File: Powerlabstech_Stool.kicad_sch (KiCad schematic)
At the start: 54 parts, among them J1 Screw_Terminal_01x02, J2 Conn_01x02_Pin, J3 Conn_01x02_Pin, J4 Conn_01x05_Socket, J5 Screw_Terminal_01x02, K1 SANYOU_SRD_Form_C, Q1 Q_NMOS_GSD, Q2 Q_NMOS_GSD, Q3 Q_NMOS_GSD, Q4 Q_NMOS_GSD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

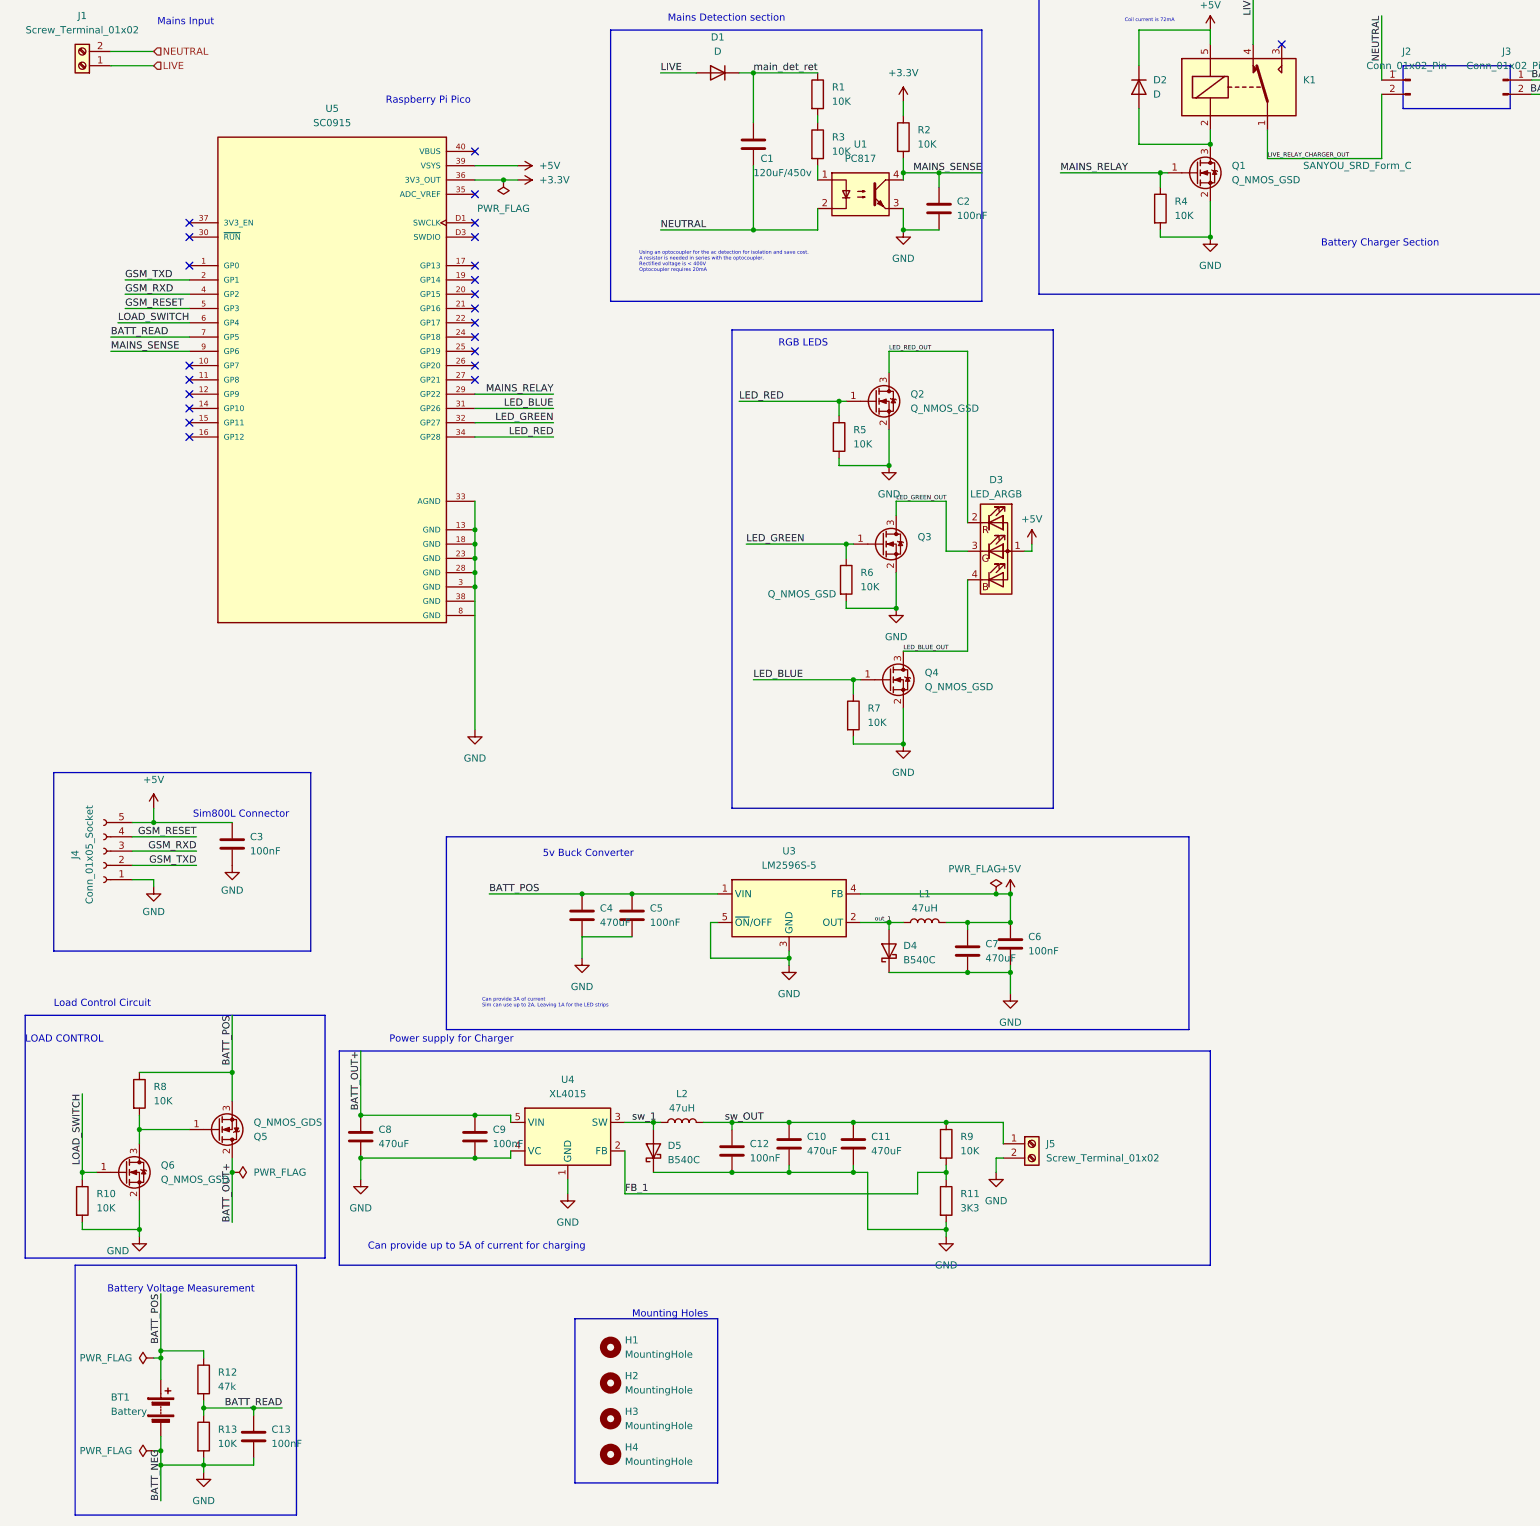
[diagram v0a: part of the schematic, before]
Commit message: Modified USB type C to supply 3A current
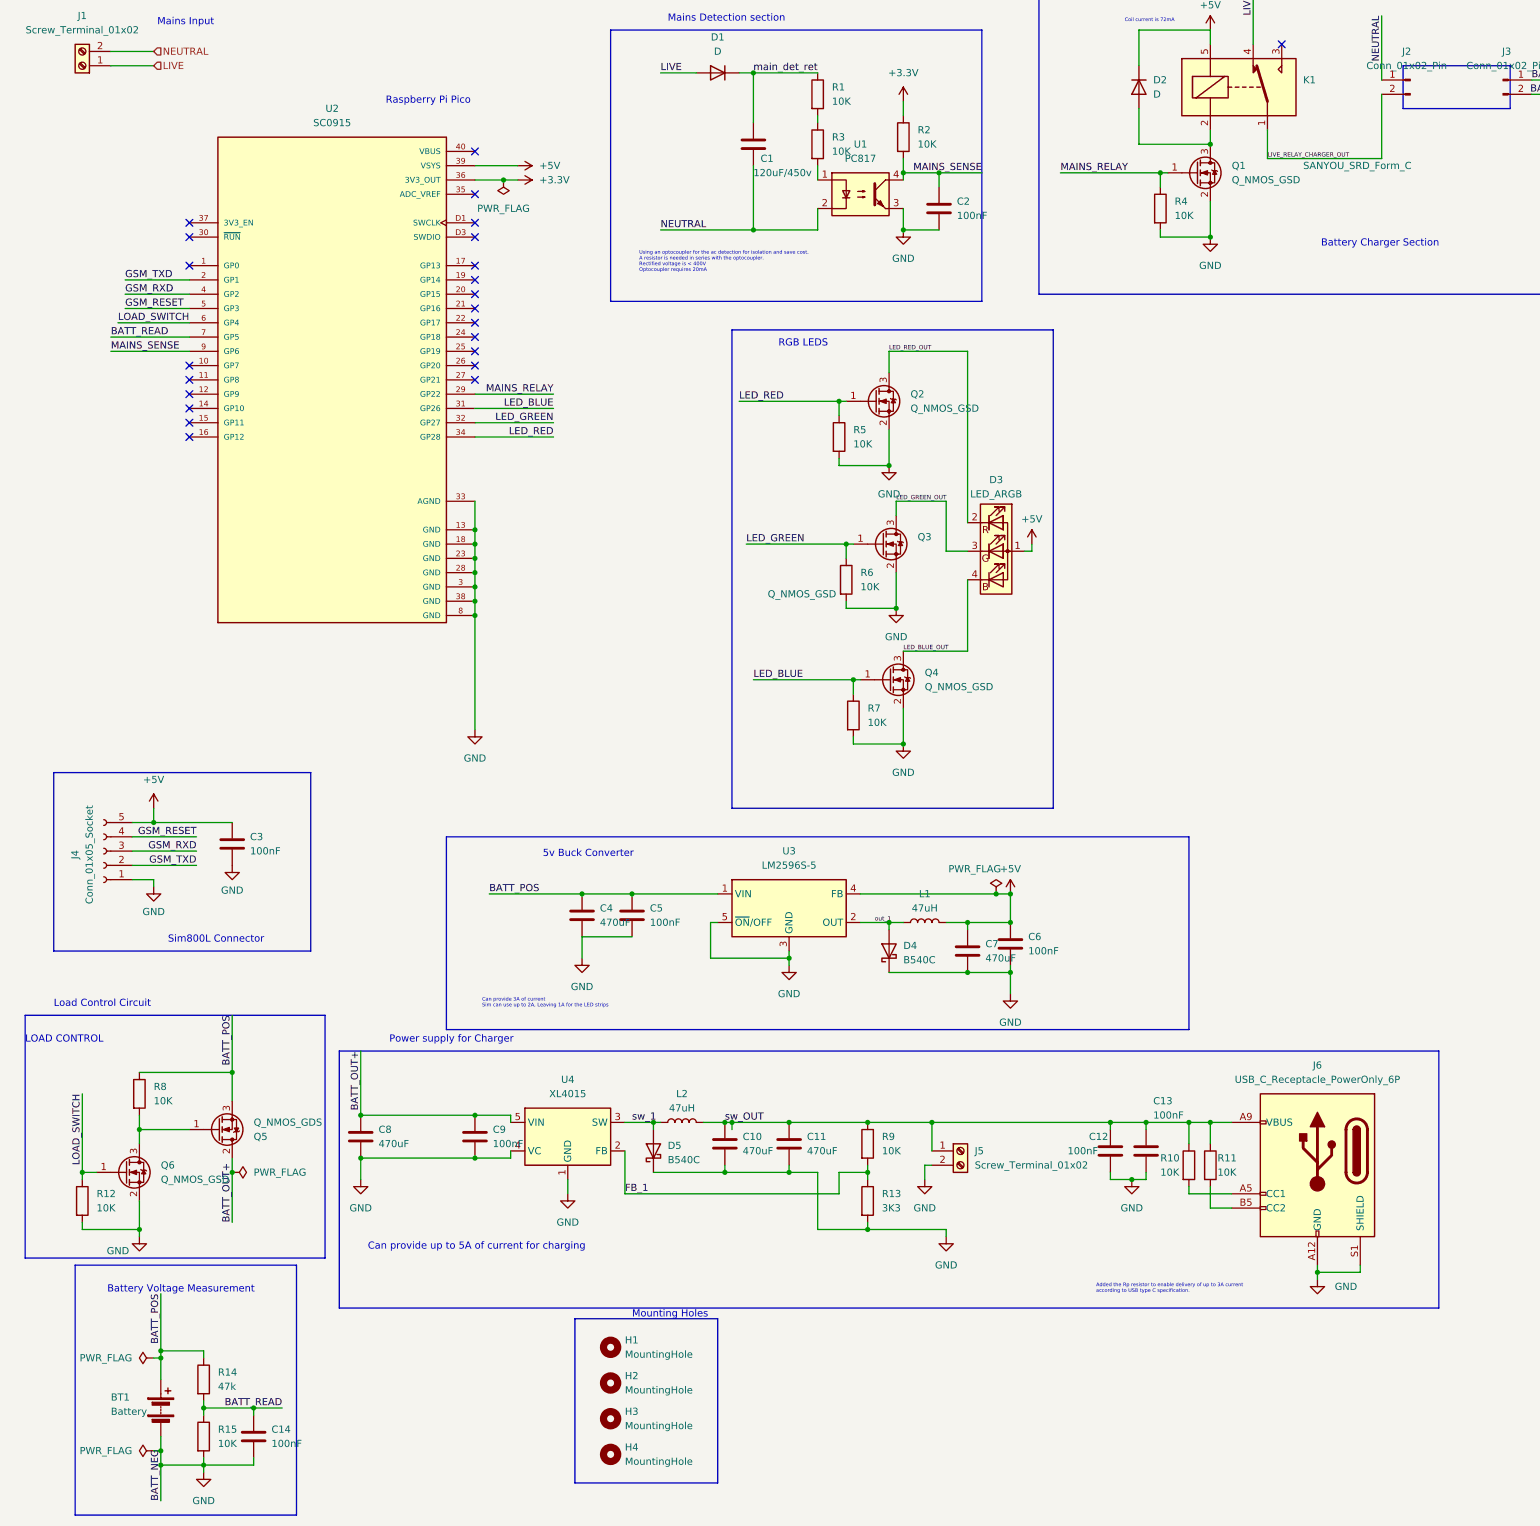
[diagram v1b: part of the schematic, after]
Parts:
- added C13: 100nF, Capacitor_SMD:C_0603_1608Metric, symbol Device:C
- added J6: USB_C_Receptacle_PowerOnly_6P, Connector_USB:USB_C_Receptacle_GCT_USB4125-xx-x_6P_TopMnt_Horizontal, symbol Connector:USB_C_Receptacle_PowerOnly_6P
- added R10, R11: 10K, Resistor_SMD:R_0603_1608Metric, symbol Device:R
- D3: footprint TerminalBlock:TerminalBlock_bornier-4_P5.08mm -> TerminalBlock_Phoenix:TerminalBlock_Phoenix_MKDS-3-4-5.08_1x04_P5.08mm_Horizontal
- renumbered C13 to C14, R10 to R12, R11 to R13, R12 to R14, R13 to R15, U5 to U2
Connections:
- net GND: now also U2.38 (GND), U2.8 (GND), C13.2, J6.A12 (GND), J6.B12 (GND), J6.S1 (SHIELD)
- net sw_OUT: now also C13.1, J6.A9 (VBUS), J6.B9 (VBUS), R10.1, R11.1
- new net: J6.B5 (CC2), R11.2
- new net: J6.A5 (CC1), R10.2
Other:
- note added: "Added the Rp resistor to enable delivery of up to 3A current according to USB type C specification."
- moved on the sheet: C10, C11, C12, J5, R13, R9
